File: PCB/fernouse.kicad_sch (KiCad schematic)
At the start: 2 parts, among them J1 USB_C_Receptacle, U1 nRF52840

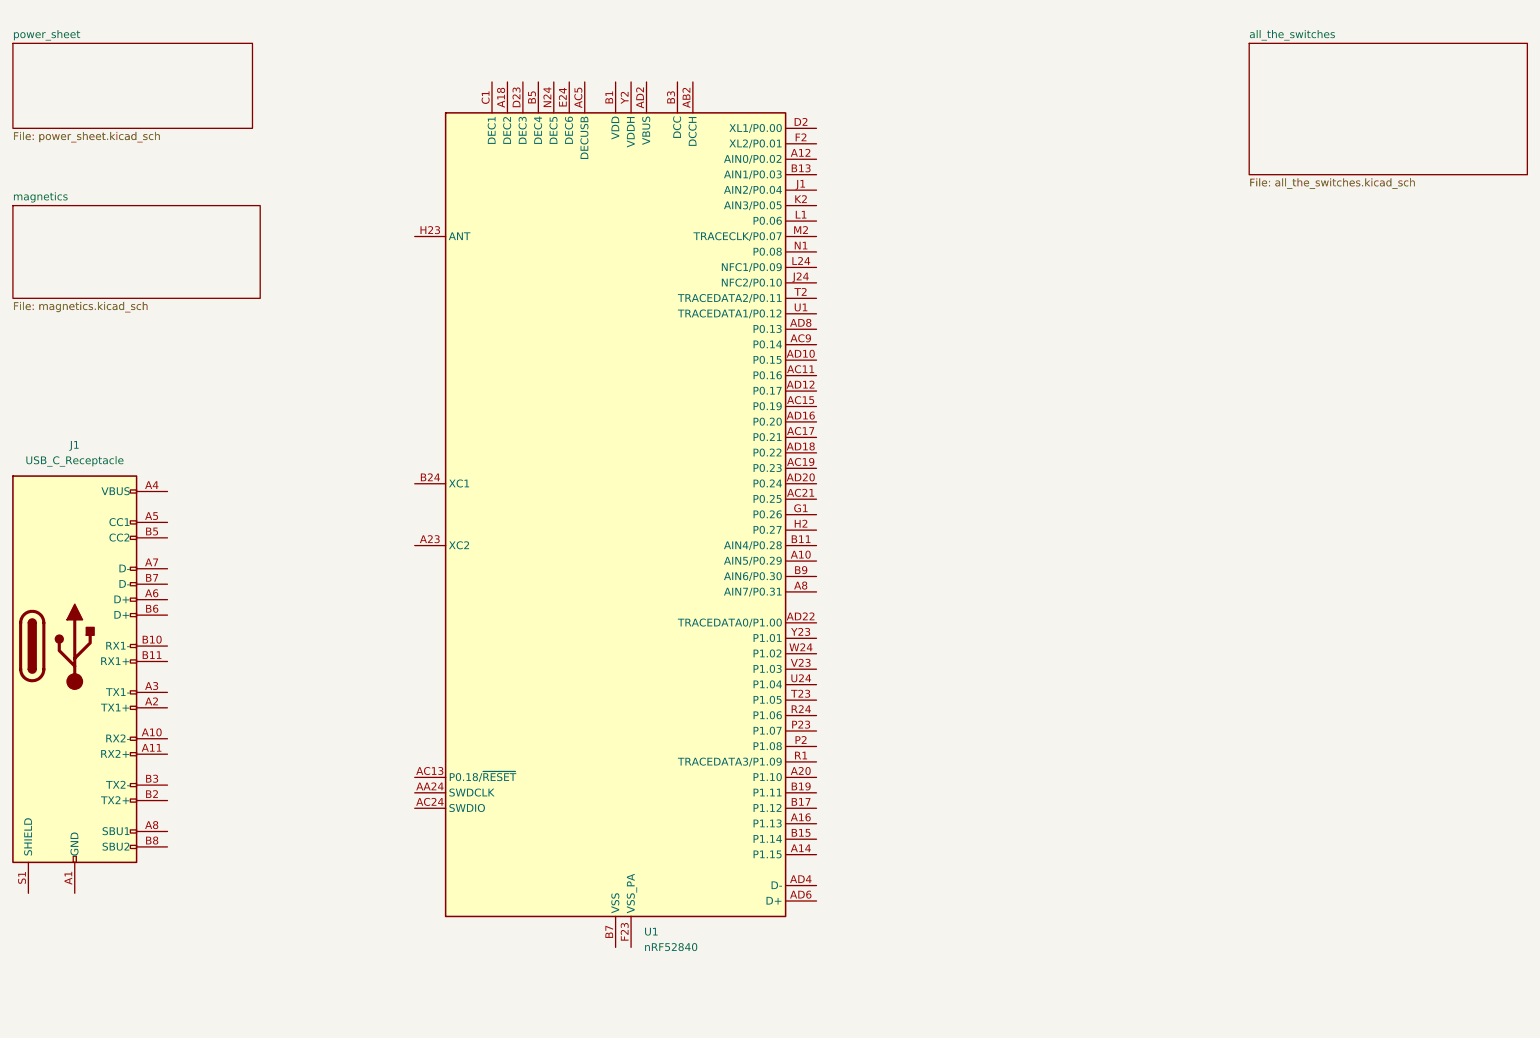
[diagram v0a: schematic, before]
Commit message: realized the magnetic sensor wont work because of orientation
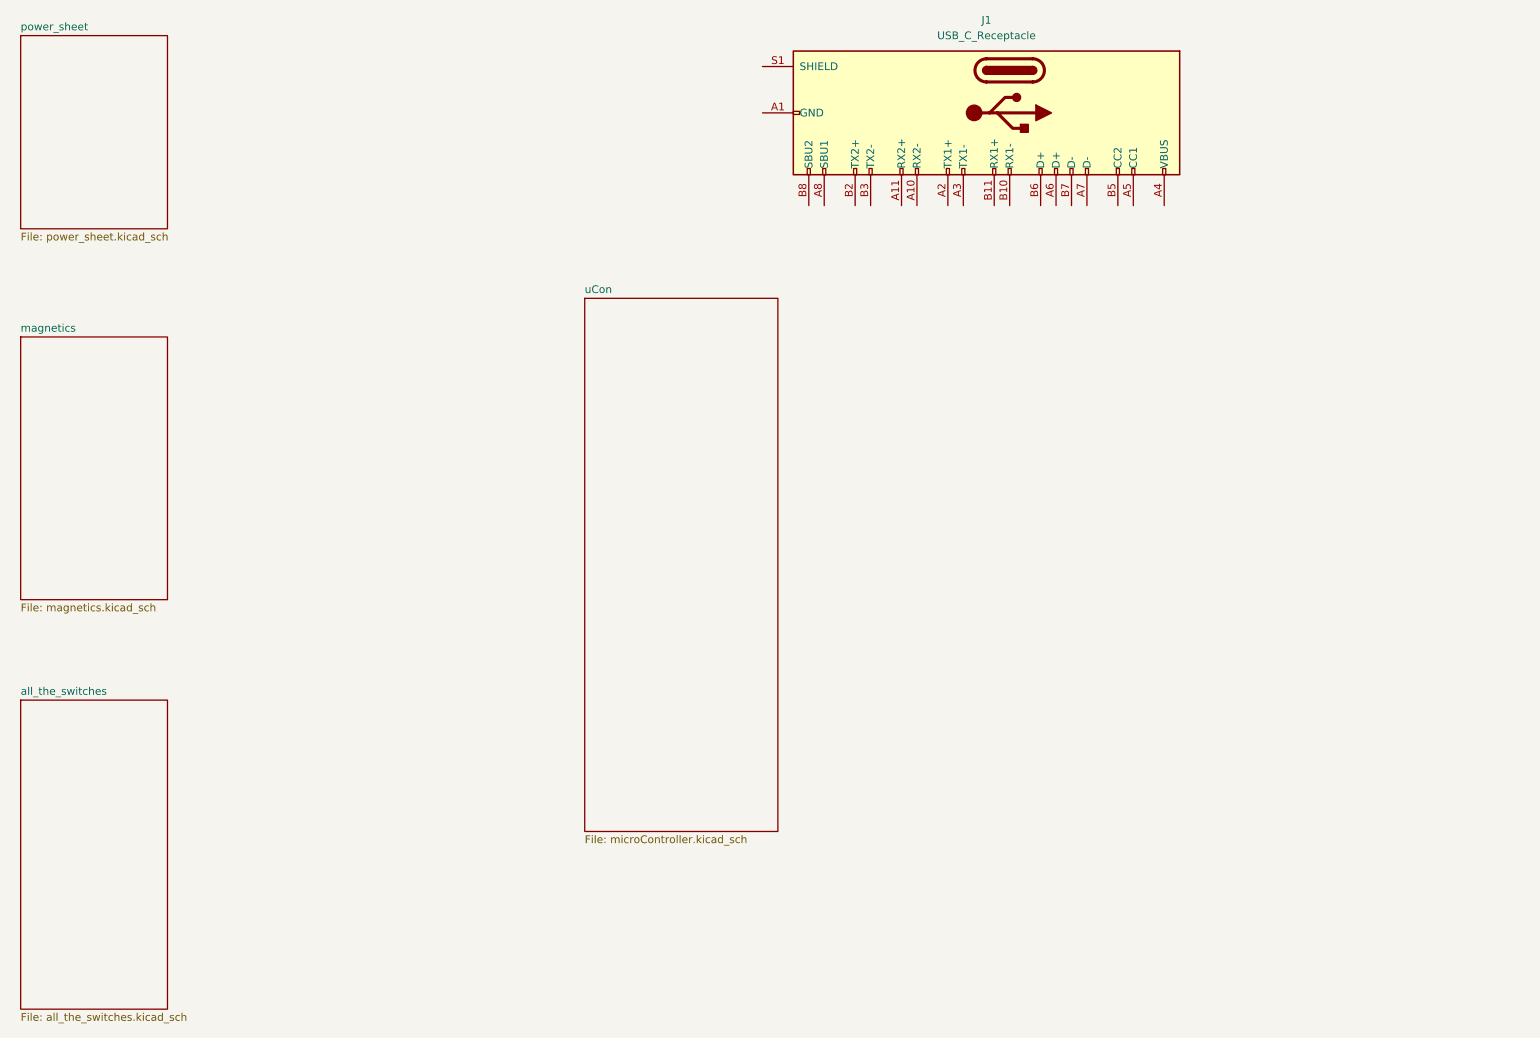
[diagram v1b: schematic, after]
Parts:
- removed U1: nRF52840, Package_DFN_QFN:Nordic_AQFN-73-1EP_7x7mm_P0.5mm, symbol MCU_Nordic:nRF52840
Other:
- added sheet uCon (microController.kicad_sch)
- moved on the sheet: J1
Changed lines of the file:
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@@
 	(paper "A4")
 	(symbol
-		(lib_id "MCU_Nordic:nRF52840")
-		(at 123.19 96.52 0)
+		(lib_id "Connector:USB_C_Receptacle")
+		(at 187.96 30.48 270)
 		(unit 1)
 		(exclude_from_sim no)
@@
 		(dnp no)
 		(fields_autoplaced yes)
-		(property "Reference" "U1"
-			(at 127.8733 165.1 0)
-			(effects
-				(font
-					(size 1.27 1.27)
-				)
-				(justify left)
-			)
-		)
-		(property "Value" "nRF52840"
-			(at 127.8733 167.64 0)
-			(effects
-				(font
-					(size 1.27 1.27)
-				)
-				(justify left)
-			)
-		)
-		(property "Footprint" "Package_DFN_QFN:Nordic_AQFN-73-1EP_7x7mm_P0.5mm"
-			(at 123.19 170.18 0)
+		(property "Reference" "J1"
+			(at 184.15 15.24 90)
+			(effects
+				(font
+					(size 1.27 1.27)
+				)
+			)
+		)
+		(property "Value" "USB_C_Receptacle"
+			(at 184.15 17.78 90)
+			(effects
+				(font
+					(size 1.27 1.27)
+				)
+			)
+		)
+		(property "Footprint" ""
+			(at 187.96 34.29 0)
 			(effects
 				(font
@@
 			)
 		)
-		(property "Datasheet" "http://infocenter.nordicsemi.com/topic/com.nordic.infocenter.nrf52/dita/nrf52/chips/nrf52840.html"
-			(at 106.68 48.26 0)
+		(property "Datasheet" "https://www.usb.org/sites/default/files/documents/usb_type-c.zip"
+			(at 187.96 34.29 0)
 			(effects
 				(font
@@
 			)
 		)
-		(property "Description" "Multiprotocol BLE/ANT/2.4 GHz/802.15.4 Cortex-M4F SoC, AQFN-73"
-			(at 123.19 96.52 0)
-			(effects
-				(font
-					(size 1.27 1.27)
-				)
-				(hide yes)
-			)
-		)
-		(pin "B19"
-		)
-		(pin "A16"
-		)
-		(pin "B15"
-		)
-		(pin "AD4"
-		)
-		(pin "A20"
-		)
-		(pin "A14"
-		)
-		(pin "B17"
-		)
-		(pin "AD6"
-		)
-		(pin "A18"
-		)
-		(pin "E24"
-		)
-		(pin "AC5"
-		)
-		(pin "D23"
-		)
-		(pin "B24"
-		)
-		(pin "W1"
-		)
-		(pin "AA24"
-		)
-		(pin "A23"
-		)
-		(pin "F23"
-		)
-		(pin "B7"
-		)
-		(pin "B1"
-		)
-		(pin "AC24"
-		)
-		(pin "H23"
-		)
-		(pin "AC13"
-		)
-		(pin "C1"
-		)
-		(pin "B5"
-		)
-		(pin "N24"
-		)
-		(pin "AD14"
-		)
-		(pin "A22"
-		)
-		(pin "AD23"
-		)
-		(pin "EP"
-		)
-		(pin "Y2"
-		)
-		(pin "AD2"
-		)
-		(pin "J24"
-		)
-		(pin "U1"
-		)
-		(pin "AC9"
-		)
-		(pin "N1"
-		)
-		(pin "AC11"
-		)
-		(pin "AD16"
-		)
-		(pin "L24"
-		)
-		(pin "F2"
-		)
-		(pin "AD8"
-		)
-		(pin "AD10"
-		)
-		(pin "AD12"
-		)
-		(pin "AC15"
-		)
-		(pin "D2"
-		)
-		(pin "B3"
-		)
-		(pin "B13"
-		)
-		(pin "J1"
-		)
-		(pin "K2"
-		)
-		(pin "M2"
-		)
-		(pin "T2"
-		)
-		(pin "L1"
-		)
-		(pin "A12"
-		)
-		(pin "AB2"
-		)
-		(pin "P23"
-		)
-		(pin "T23"
-		)
-		(pin "P2"
-		)
-		(pin "R1"
-		)
-		(pin "AD18"
-		)
-		(pin "AC17"
-		)
-		(pin "AC19"
-		)
-		(pin "H2"
-		)
-		(pin "B11"
-		)
-		(pin "B9"
-		)
-		(pin "A8"
-		)
-		(pin "Y23"
-		)
-		(pin "V23"
-		)
-		(pin "A10"
-		)
-		(pin "G1"
-		)
-		(pin "AD20"
-		)
-		(pin "AD22"
-		)
-		(pin "AC21"
-		)
-		(pin "W24"
-		)
-		(pin "U24"
-		)
-		(pin "R24"
-		)
-		(instances
-			(project ""
-				(path "/676a96c8-df44-4067-be01-152bfa3def97"
-					(reference "U1")
-					(unit 1)
-				)
-			)
-		)
-	)
-	(symbol
-		(lib_id "Connector:USB_C_Receptacle")
-		(at 34.29 118.11 0)
-		(unit 1)
-		(exclude_from_sim no)
-		(in_bom yes)
-		(on_board yes)
-		(dnp no)
-		(fields_autoplaced yes)
-		(property "Reference" "J1"
-			(at 34.29 85.09 0)
-			(effects
-				(font
-					(size 1.27 1.27)
-				)
-			)
-		)
-		(property "Value" "USB_C_Receptacle"
-			(at 34.29 87.63 0)
-			(effects
-				(font
-					(size 1.27 1.27)
-				)
-			)
-		)
-		(property "Footprint" ""
-			(at 38.1 118.11 0)
-			(effects
-				(font
-					(size 1.27 1.27)
-				)
-				(hide yes)
-			)
-		)
-		(property "Datasheet" "https://www.usb.org/sites/default/files/documents/usb_type-c.zip"
-			(at 38.1 118.11 0)
-			(effects
-				(font
-					(size 1.27 1.27)
-				)
-				(hide yes)
-			)
-		)
 		(property "Description" "USB Full-Featured Type-C Receptacle connector"
-			(at 34.29 118.11 0)
+			(at 187.96 30.48 0)
 			(effects
 				(font
@@
 	)
 	(sheet
-		(at 24.13 45.72)
-		(size 40.64 15.24)
+		(at 25.4 67.31)
+		(size 24.13 43.18)
 		(exclude_from_sim no)
 		(in_bom yes)
@@
 		)
 		(property "Sheetname" "magnetics"
-			(at 24.13 45.0084 0)
+			(at 25.4 66.5984 0)
 			(effects
 				(font
@@
 		)
 		(property "Sheetfile" "magnetics.kicad_sch"
-			(at 24.13 61.5446 0)
+			(at 25.4 111.0746 0)
 			(effects
 				(font
@@
 	)
 	(sheet
-		(at 227.33 19.05)
-		(size 45.72 21.59)
+		(at 118.11 60.96)
+		(size 31.75 87.63)
+		(exclude_from_sim no)
+		(in_bom yes)
+		(on_board yes)
+		(dnp no)
+		(fields_autoplaced yes)
+		(stroke
+			(width 0.1524)
+			(type solid)
+		)
+		(fill
+			(color 0 0 0 0.0000)
+		)
+		(property "Sheetname" "uCon"
+			(at 118.11 60.2484 0)
+			(effects
+				(font
+					(size 1.27 1.27)
+				)
+				(justify left bottom)
+			)
+		)
+		(property "Sheetfile" "microController.kicad_sch"
+			(at 118.11 149.1746 0)
+			(effects
+				(font
+					(size 1.27 1.27)
+				)
+				(justify left top)
+			)
+		)
+		(instances
+			(project "fernouse"
+				(path "/676a96c8-df44-4067-be01-152bfa3def97"
+					(page "5")
+				)
+			)
+		)
+	)
+	(sheet
+		(at 25.4 127)
+		(size 24.13 50.8)
 		(exclude_from_sim no)
 		(in_bom yes)
@@
 		)
 		(property "Sheetname" "all_the_switches"
-			(at 227.33 18.3384 0)
+			(at 25.4 126.2884 0)
 			(effects
 				(font
@@
 		)
 		(property "Sheetfile" "all_the_switches.kicad_sch"
-			(at 227.33 41.2246 0)
+			(at 25.4 178.3846 0)
 			(effects
 				(font
@@
 	)
 	(sheet
-		(at 24.13 19.05)
-		(size 39.37 13.97)
+		(at 25.4 17.78)
+		(size 24.13 31.75)
 		(exclude_from_sim no)
 		(in_bom yes)
@@
 		)
 		(property "Sheetname" "power_sheet"
-			(at 24.13 18.3384 0)
+			(at 25.4 17.0684 0)
 			(effects
 				(font
@@
 		)
 		(property "Sheetfile" "power_sheet.kicad_sch"
-			(at 24.13 33.6046 0)
-			(effects
-				(font
+			(at 25.4 50.1146 0)
+			(effects
+				(font

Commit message: adding secondary pcb for magnetic field sensor
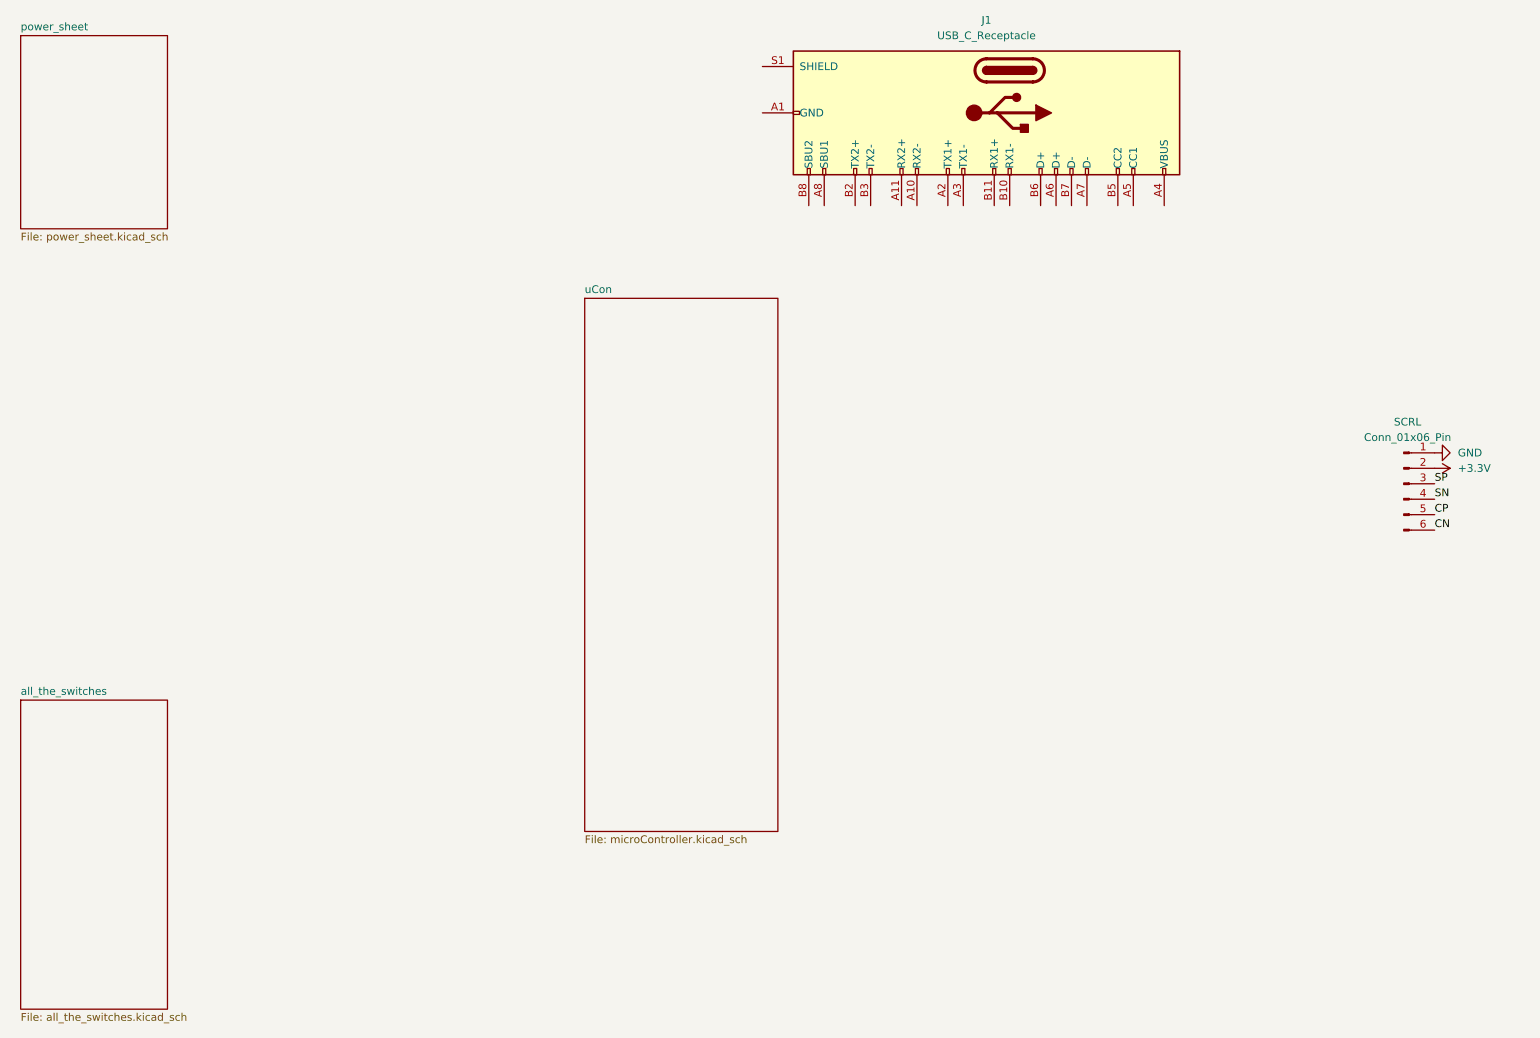
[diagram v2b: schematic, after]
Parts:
- added SCRL: Conn_01x06_Pin, Connector_PinHeader_1.00mm:PinHeader_1x06_P1.00mm_Vertical, symbol Connector:Conn_01x06_Pin
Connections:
- new net +3.3V: SCRL.2 (Pin_2)
- new net CN: SCRL.6 (Pin_6)
- new net CP: SCRL.5 (Pin_5)
- new net GND: SCRL.1 (Pin_1)
- new net SN: SCRL.4 (Pin_4)
- new net SP: SCRL.3 (Pin_3)
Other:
- removed sheet magnetics
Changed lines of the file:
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@@
 	(generator_version "9.0")
 	(paper "A4")
+	(label "SP"
+		(at 257.81 91.44 0)
+		(effects
+			(font
+				(size 1.27 1.27)
+			)
+			(justify left bottom)
+		)
+	)
+	(label "CN"
+		(at 257.81 99.06 0)
+		(effects
+			(font
+				(size 1.27 1.27)
+			)
+			(justify left bottom)
+		)
+	)
+	(label "CP"
+		(at 257.81 96.52 0)
+		(effects
+			(font
+				(size 1.27 1.27)
+			)
+			(justify left bottom)
+		)
+	)
+	(label "SN"
+		(at 257.81 93.98 0)
+		(effects
+			(font
+				(size 1.27 1.27)
+			)
+			(justify left bottom)
+		)
+	)
+	(symbol
+		(lib_id "Connector:Conn_01x06_Pin")
+		(at 252.73 91.44 0)
+		(unit 1)
+		(exclude_from_sim no)
+		(in_bom yes)
+		(on_board yes)
+		(dnp no)
+		(fields_autoplaced yes)
+		(property "Reference" "SCRL"
+			(at 253.365 81.28 0)
+			(effects
+				(font
+					(size 1.27 1.27)
+				)
+			)
+		)
+		(property "Value" "Conn_01x06_Pin"
+			(at 253.365 83.82 0)
+			(effects
+				(font
+					(size 1.27 1.27)
+				)
+			)
+		)
+		(property "Footprint" "Connector_PinHeader_1.00mm:PinHeader_1x06_P1.00mm_Vertical"
+			(at 252.73 91.44 0)
+			(effects
+				(font
+					(size 1.27 1.27)
+				)
+				(hide yes)
+			)
+		)
+		(property "Datasheet" "~"
+			(at 252.73 91.44 0)
+			(effects
+				(font
+					(size 1.27 1.27)
+				)
+				(hide yes)
+			)
+		)
+		(property "Description" "Generic connector, single row, 01x06, script generated"
+			(at 252.73 91.44 0)
+			(effects
+				(font
+					(size 1.27 1.27)
+				)
+				(hide yes)
+			)
+		)
+		(pin "3"
+		)
+		(pin "6"
+		)
+		(pin "1"
+		)
+		(pin "2"
+		)
+		(pin "4"
+		)
+		(pin "5"
+		)
+		(instances
+			(project ""
+				(path "/676a96c8-df44-4067-be01-152bfa3def97"
+					(reference "SCRL")
+					(unit 1)
+				)
+			)
+		)
+	)
 	(symbol
 		(lib_id "Connector:USB_C_Receptacle")
@@
 		)
 	)
-	(sheet
-		(at 25.4 67.31)
-		(size 24.13 43.18)
+	(symbol
+		(lib_id "power:GND")
+		(at 257.81 86.36 90)
+		(unit 1)
 		(exclude_from_sim no)
 		(in_bom yes)
@@
 		(dnp no)
 		(fields_autoplaced yes)
-		(stroke
-			(width 0.1524)
-			(type solid)
-		)
-		(fill
-			(color 0 0 0 0.0000)
-		)
-		(property "Sheetname" "magnetics"
-			(at 25.4 66.5984 0)
-			(effects
-				(font
-					(size 1.27 1.27)
-				)
-				(justify left bottom)
-			)
-		)
-		(property "Sheetfile" "magnetics.kicad_sch"
-			(at 25.4 111.0746 0)
-			(effects
-				(font
-					(size 1.27 1.27)
-				)
-				(justify left top)
-			)
+		(property "Reference" "#PWR02"
+			(at 264.16 86.36 0)
+			(effects
+				(font
+					(size 1.27 1.27)
+				)
+				(hide yes)
+			)
+		)
+		(property "Value" "GND"
+			(at 261.62 86.3599 90)
+			(effects
+				(font
+					(size 1.27 1.27)
+				)
+				(justify right)
+			)
+		)
+		(property "Footprint" ""
+			(at 257.81 86.36 0)
+			(effects
+				(font
+					(size 1.27 1.27)
+				)
+				(hide yes)
+			)
+		)
+		(property "Datasheet" ""
+			(at 257.81 86.36 0)
+			(effects
+				(font
+					(size 1.27 1.27)
+				)
+				(hide yes)
+			)
+		)
+		(property "Description" "Power symbol creates a global label with name \"GND\" , ground"
+			(at 257.81 86.36 0)
+			(effects
+				(font
+					(size 1.27 1.27)
+				)
+				(hide yes)
+			)
+		)
+		(pin "1"
 		)
 		(instances
-			(project "fernouse"
+			(project ""
 				(path "/676a96c8-df44-4067-be01-152bfa3def97"
-					(page "3")
-				)
-			)
+					(reference "#PWR02")
+					(unit 1)
+				)
+			)
+		)
+	)
+	(symbol
+		(lib_id "power:+3.3V")
+		(at 257.81 88.9 270)
+		(unit 1)
+		(exclude_from_sim no)
+		(in_bom yes)
+		(on_board yes)
+		(dnp no)
+		(fields_autoplaced yes)
+		(property "Reference" "#PWR01"
+			(at 254 88.9 0)
+			(effects
+				(font
+					(size 1.27 1.27)
+				)
+				(hide yes)
+			)
+		)
+		(property "Value" "+3.3V"
+			(at 261.62 88.8999 90)
+			(effects
+				(font
+					(size 1.27 1.27)
+				)
+				(justify left)
+			)
+		)
+		(property "Footprint" ""
+			(at 257.81 88.9 0)
+			(effects
+				(font
+					(size 1.27 1.27)
+				)
+				(hide yes)
+			)
+		)
+		(property "Datasheet" ""
+			(at 257.81 88.9 0)
+			(effects
+				(font
+					(size 1.27 1.27)
+				)
+				(hide yes)
+			)
+		)
+		(property "Description" "Power symbol creates a global label with name \"+3.3V\""
+			(at 257.81 88.9 0)
+			(effects
+				(font
+					(size 1.27 1.27)
+				)
+				(hide yes)
+			)
+		)
+		(pin "1"
+		)
+		(instances
+			(project ""
+				(path "/676a96c8-df44-4067-be01-152bfa3def97"
+					(reference "#PWR01")
+					(unit 1)
+				)
+			)
